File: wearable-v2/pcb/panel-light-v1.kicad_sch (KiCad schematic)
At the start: 4 parts, among them J5 PNL_1_SOCKET, U9 APDS-9250

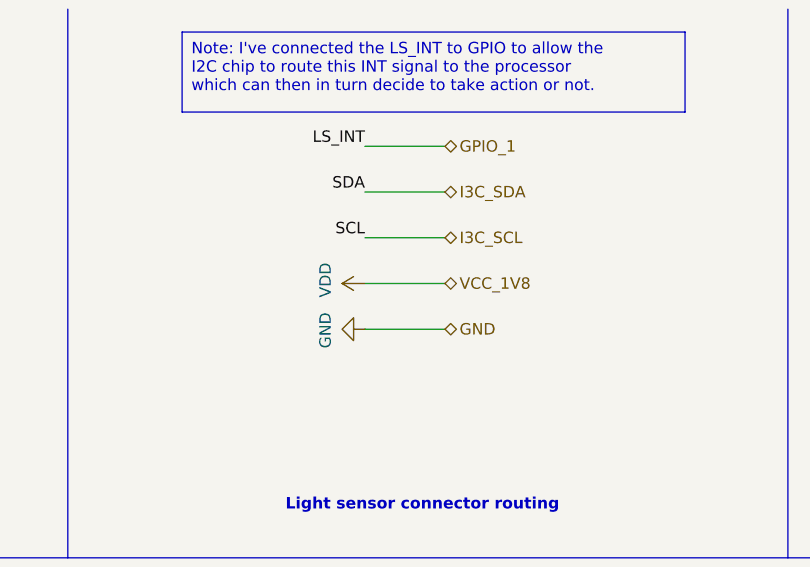
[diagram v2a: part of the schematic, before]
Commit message: Corrected 1V8 routing to bio board
Signed-off-by: Adam Fowler <adam@adamfowler.org>
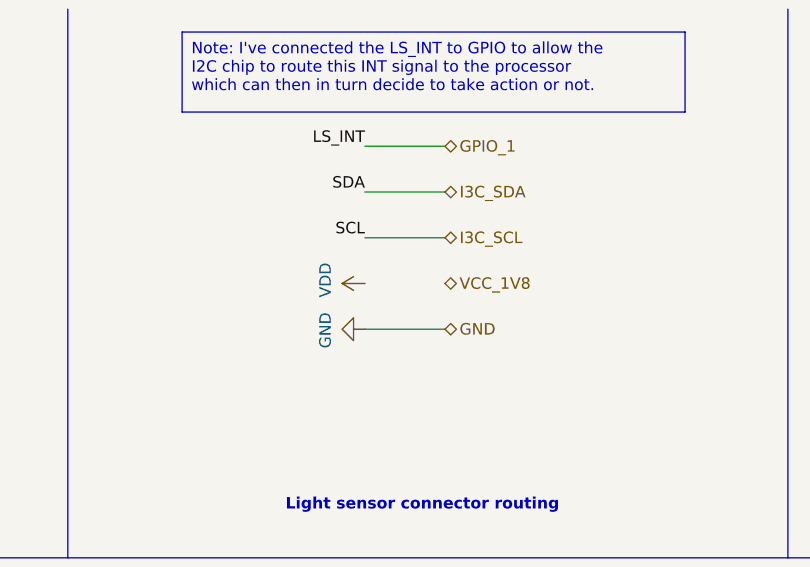
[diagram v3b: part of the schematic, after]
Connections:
- net VDD: no longer J5.2 (Pin_2)
- new net VCC_1V8: J5.2 (Pin_2)
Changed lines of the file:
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@@
-    (stroke (width 0) (type default))
-  )
-  (wire (pts (xy 157.48 44.45) (xy 166.37 44.45))
     (stroke (width 0) (type default))
   )

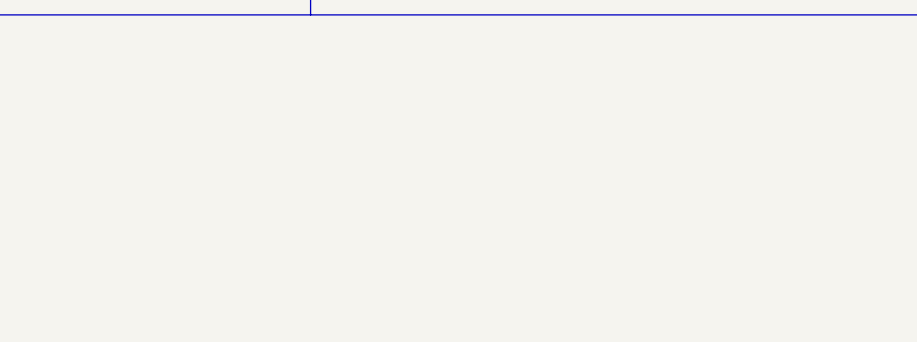
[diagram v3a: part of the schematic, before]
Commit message: Added I2C and I3C notes and additional resistors
Signed-off-by: Adam Fowler <adam@adamfowler.org>
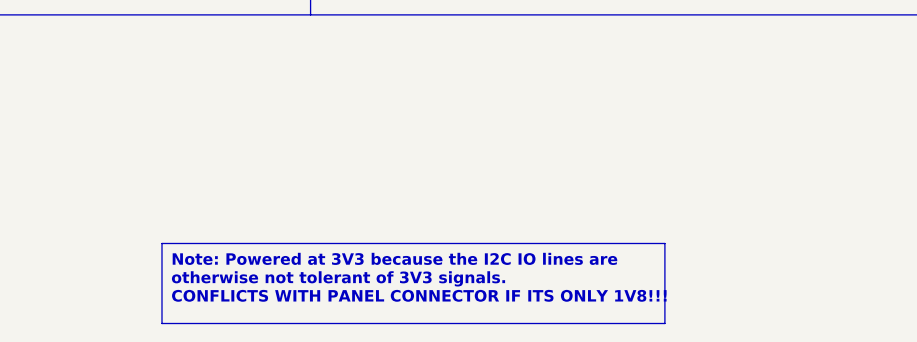
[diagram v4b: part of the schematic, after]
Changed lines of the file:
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@@
     (effects (font (size 1.27 1.27)) (justify left top))
+  )
+  (text_box "Note: Powered at 3V3 because the I2C IO lines are otherwise not tolerant of 3V3 signals.\nCONFLICTS WITH PANEL CONNECTOR IF ITS ONLY 1V8!!!"
+    (at 107.95 100.33 0) (size 55.88 8.89)
+    (stroke (width 0) (type default))
+    (fill (type none))
+    (effects (font (size 1.27 1.27) bold) (justify left top))
   )
   (text "optional" (at 77.47 27.94 0)
@@
       (effects (font (size 1.27 1.27)) hide)
     )
-    (property "Datasheet" "https://docs.broadcom.com/doc/AV02-4733EN" (at 80.01 36.83 0)
-      (effects (font (size 1.27 1.27)) hide)
-    )
+    (property "Datasheet" "https://docs.broadcom.com/doc/APDS-9250-Digital-RGB-IR-Ambient-Light-Sensor-DS" (at 80.01 36.83 0)
+      (effects (font (size 1.27 1.27)) hide)
+    )
